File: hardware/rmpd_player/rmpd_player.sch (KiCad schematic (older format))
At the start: 54 parts

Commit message: ds3231 stubs added
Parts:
- added BT?: CR2032, symbol Device:Battery_Cell
- added C?: 100n, symbol Device:C
- added U?: DS3231M, Package_SO:SOIC-16W_7.5x10.3mm_P1.27mm, symbol Timer_RTC:DS3231M
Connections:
- net labels added: I2C_SCL, I2C_SDA, TRANSIENT_MUTE
- net labels removed: MUTE
- wire segments 235 -> 247
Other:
- moved on the sheet: R?

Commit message: annotate schematic
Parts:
- removed J?: Micro_SD_Card_Det, symbol Connector:Micro_SD_Card_Det
- removed J?: AudioJack3_Ground, symbol Connector:AudioJack3_Ground
- added J2: PROG, Pin_Headers:Pin_Header_Straight_1x06_Pitch2.54mm, symbol Connector_Generic:Conn_01x06
- added J3: LINE_OUT_INT, Pin_Headers:Pin_Header_Straight_1x04_Pitch2.54mm, symbol Connector_Generic:Conn_01x04
- added J4: LINE_OUT_R, symbol Connector:Conn_Coaxial
- added J5: MICRO_SD, microsd:Conn_uSDcard, symbol Connector:Micro_SD_Card
- added J6: LINE_OUT_L, symbol Connector:Conn_Coaxial
- BT1: renamed from BT?; footprint (none) -> Battery_Holders:Keystone_103_1x20mm-CoinCell
- C1, C10, C11, C13, C14, C16, C2, C3, C4, C5, C6, C7, C8, C9: renamed from C?; footprint (none) -> Capacitors_SMD:C_0805_HandSoldering
- C12, C15, C17, C18: renamed from C?; footprint (none) -> Capacitors_THT:CP_Radial_D5.0mm_P2.50mm
- D1: renamed from D?; footprint (none) -> Diodes_SMD:D_0805
- F1: renamed from F?; footprint (none) -> Fuse_Holders_and_Fuses:Fuse_SMD1206_HandSoldering
- J1: renamed from J?; value Barrel_Jack -> POWER; footprint (none) -> Connectors:BARREL_JACK
- R1, R10, R11, R12, R13, R14, R15, R16, R17, R18, R19, R2, R20, R21, R22, R23, R24, R3, R4, R5, R6, R7, R8, R9: renamed from R?; footprint (none) -> Resistors_SMD:R_0805_HandSoldering
- U3: renamed from U?; footprint (none) -> TO_SOT_Packages_SMD:SOT-223
- Y1: renamed from Y?; footprint (none) -> Crystals:Crystal_HC18-U_Vertical
- gave numbers to parts that had none: 7
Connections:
- net labels added: EN, IO0, UART_RX, UART_TX
- wire segments 247 -> 268
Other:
- moved on the sheet: BT1, C3, U1

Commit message: 2rca footprints
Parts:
- removed J4: LINE_OUT_R, symbol Connector:Conn_Coaxial
- removed J6: LINE_OUT_L, symbol Connector:Conn_Coaxial
- added J4: LINE_OUT, microsd:2RCA, symbol Connector:Conn_Coaxial_x2
- Q1, Q2, Q3, Q4: footprint Package_TO_SOT_SMD:SOT-23 -> TO_SOT_Packages_SMD:SOT-23
- U1: footprint Package_SO:SOIC-16W_7.5x10.3mm_P1.27mm -> Housings_SOIC:SOIC-16W_7.5x10.3mm_Pitch1.27mm
- U4: footprint ESP32-footprints-Lib:ESP32-WROOM -> microsd:ESP32-WROOM
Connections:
- wire segments 268 -> 264
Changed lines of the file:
@@
 F 0 "U4" H 5975 3587 60  0000 C CNN
 F 1 "ESP32-WROOM" H 5975 3481 60  0000 C CNN
-F 2 "ESP32-footprints-Lib:ESP32-WROOM" H 6350 3550 60  0001 C CNN
+F 2 "microsd:ESP32-WROOM" H 6350 3550 60  0001 C CNN
 F 3 "" H 5550 2650 60  0001 C CNN
 	1    6000 2200
@@
 	6600 5950 6450 5950
 Connection ~ 6450 5950
-Wire Wire Line
-	6600 4400 6700 4400
-Wire Wire Line
-	6700 4400 6700 4550
-Wire Wire Line
-	6700 4550 6750 4550
 Connection ~ 6600 4400
-Wire Wire Line
-	6450 5100 6700 5100
 Connection ~ 6450 5100
-Wire Wire Line
-	6600 5950 6950 5950
-Wire Wire Line
-	6950 5950 6950 5450
 Connection ~ 6600 5950
 $Comp
@@
 F 0 "Q1" H 8190 4746 50  0000 L CNN
 F 1 "BC848" H 8190 4655 50  0000 L CNN
-F 2 "Package_TO_SOT_SMD:SOT-23" H 8200 4625 50  0001 L CIN
+F 2 "TO_SOT_Packages_SMD:SOT-23" H 8200 4625 50  0001 L CIN
 F 3 "http://www.infineon.com/dgdl/Infineon-BC847SERIES_BC848SERIES_BC849SERIES_BC850SERIES-DS-v01_01-en.pdf?fileId=db3a304314dca389011541d4630a1657" H 8000 4700 50  0001 L CNN
 	1    8000 4700
@@
 F 0 "Q2" H 8590 5646 50  0000 L CNN
 F 1 "BC848" H 8590 5555 50  0000 L CNN
-F 2 "Package_TO_SOT_SMD:SOT-23" H 8600 5525 50  0001 L CIN
+F 2 "TO_SOT_Packages_SMD:SOT-23" H 8600 5525 50  0001 L CIN
 F 3 "http://www.infineon.com/dgdl/Infineon-BC847SERIES_BC848SERIES_BC849SERIES_BC850SERIES-DS-v01_01-en.pdf?fileId=db3a304314dca389011541d4630a1657" H 8400 5600 50  0001 L CNN
 	1    8400 5600
@@
 $EndComp
 Wire Wire Line
-	6700 4400 7900 4400
-Wire Wire Line
 	7900 4400 7900 4500
-Connection ~ 6700 4400
 Wire Wire Line
 	8300 5400 8300 5100
-Wire Wire Line
-	7900 5950 7250 5950
-Connection ~ 6950 5950
 Wire Wire Line
 	8300 5800 8300 5950
@@
 F 0 "Q3" H 8890 4354 50  0000 L CNN
 F 1 "BC858" H 8890 4445 50  0000 L CNN
-F 2 "Package_TO_SOT_SMD:SOT-23" H 8900 4325 50  0001 L CIN
+F 2 "TO_SOT_Packages_SMD:SOT-23" H 8900 4325 50  0001 L CIN
 F 3 "http://www.fairchildsemi.com/ds/BC/BC856.pdf" H 8700 4400 50  0001 L CNN
 	1    8700 4400
@@
 F 0 "Q4" H 9290 5254 50  0000 L CNN
 F 1 "BC858" H 9290 5345 50  0000 L CNN
-F 2 "Package_TO_SOT_SMD:SOT-23" H 9300 5225 50  0001 L CIN
+F 2 "TO_SOT_Packages_SMD:SOT-23" H 9300 5225 50  0001 L CIN
 F 3 "http://www.fairchildsemi.com/ds/BC/BC856.pdf" H 9100 5300 50  0001 L CNN
 	1    9100 5300
@@
 F 0 "U1" H 1650 1250 50  0000 C CNN
 F 1 "DS3231M" H 1650 1150 50  0000 C CNN
-F 2 "Package_SO:SOIC-16W_7.5x10.3mm_P1.27mm" H 1950 1000 50  0001 C CNN
+F 2 "Housings_SOIC:SOIC-16W_7.5x10.3mm_Pitch1.27mm" H 1950 1000 50  0001 C CNN
 F 3 "http://datasheets.maximintegrated.com/en/ds/DS3231.pdf" H 2220 1650 50  0001 C CNN
 	1    1950 1600
@@
 	1    0    0    -1
 $EndComp
-$Comp
-L Connector:Conn_Coaxial J4
-U 1 1 5C0DDCCD
-P 6950 4550
-F 0 "J4" H 6950 4850 50  0000 L CNN
-F 1 "LINE_OUT_R" H 6800 4750 50  0000 L CNN
-F 2 "" H 6950 4550 50  0001 C CNN
-F 3 " ~" H 6950 4550 50  0001 C CNN
-	1    6950 4550
-	1    0    0    -1
-$EndComp
-$Comp
-L Connector:Conn_Coaxial J6
-U 1 1 5C0DDDB1
-P 6950 5250
-F 0 "J6" H 6900 5550 50  0000 L CNN
-F 1 "LINE_OUT_L" H 6800 5450 50  0000 L CNN
-F 2 "" H 6950 5250 50  0001 C CNN
-F 3 " ~" H 6950 5250 50  0001 C CNN
-	1    6950 5250
-	1    0    0    -1
-$EndComp
-Wire Wire Line
-	6750 5250 6700 5250
-Wire Wire Line
-	6700 5250 6700 5100
-Connection ~ 6700 5100
-Wire Wire Line
-	6700 5100 8300 5100
-Wire Wire Line
-	6950 4750 6950 4800
-Wire Wire Line
-	6950 4800 7250 4800
-Wire Wire Line
-	7250 4800 7250 5950
-Connection ~ 7250 5950
-Wire Wire Line
-	7250 5950 6950 5950
+Wire Wire Line
+	6600 4400 6750 4400
+Wire Wire Line
+	6600 5950 7100 5950
+Wire Wire Line
+	6450 5100 6750 5100
+$Comp
+L Connector:Conn_Coaxial_x2 J4
+U 1 1 5C0CC33D
+P 7100 4650
+F 0 "J4" H 7200 4450 50  0000 L CNN
+F 1 "LINE_OUT" H 7200 4350 50  0000 L CNN
+F 2 "microsd:2RCA" H 7100 4550 50  0001 C CNN
+F 3 " ~" H 7100 4550 50  0001 C CNN
+	1    7100 4650
+	1    0    0    -1
+$EndComp
+Wire Wire Line
+	6900 4550 6750 4550
+Wire Wire Line
+	6750 4550 6750 4400
+Connection ~ 6750 4400
+Wire Wire Line
+	6750 4400 7900 4400
+Wire Wire Line
+	6900 4750 6750 4750
+Wire Wire Line
+	6750 4750 6750 5100
+Connection ~ 6750 5100
+Wire Wire Line
+	6750 5100 8300 5100
+Wire Wire Line
+	7100 4950 7100 5950
+Connection ~ 7100 5950
+Wire Wire Line
+	7100 5950 7900 5950
 $EndSCHEMATC

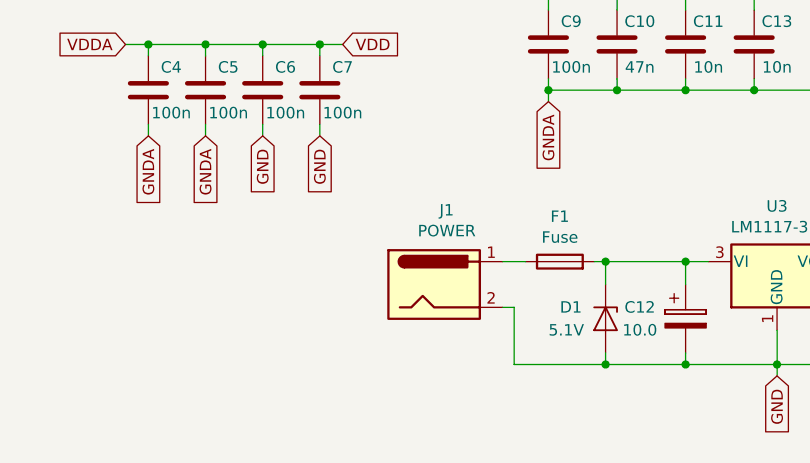
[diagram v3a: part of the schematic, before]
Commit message: power_int pinheader
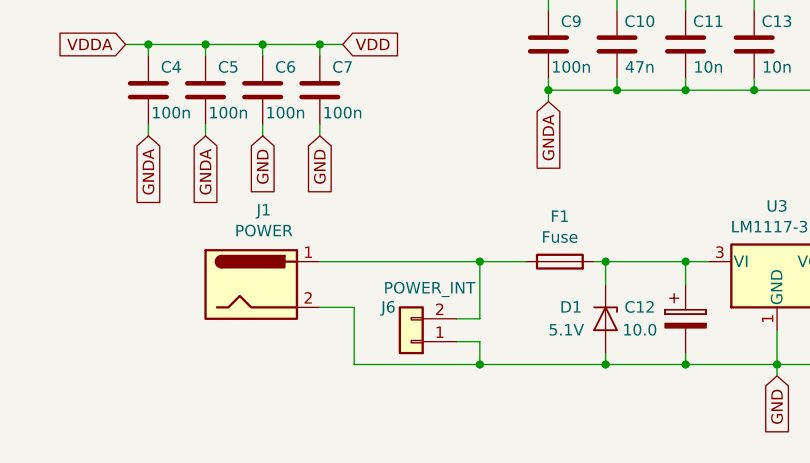
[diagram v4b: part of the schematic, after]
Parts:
- added J6: POWER_INT, Pin_Headers:Pin_Header_Straight_1x02_Pitch2.54mm, symbol Connector_Generic:Conn_01x02
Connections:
- net GND: now also J6.1 (Pin_1)
- net at F1.1, J1.1: now also J6.2 (Pin_2)
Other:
- moved on the sheet: J1
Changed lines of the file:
@@
 L Connector:Barrel_Jack J1
 U 1 1 5C11E4C3
-P 3950 6800
-F 0 "J1" H 4005 7125 50  0000 C CNN
-F 1 "POWER" H 4005 7034 50  0000 C CNN
-F 2 "Connectors:BARREL_JACK" H 4000 6760 50  0001 C CNN
-F 3 "~" H 4000 6760 50  0001 C CNN
-	1    3950 6800
+P 3150 6800
+F 0 "J1" H 3205 7125 50  0000 C CNN
+F 1 "POWER" H 3205 7034 50  0000 C CNN
+F 2 "Connectors:BARREL_JACK" H 3200 6760 50  0001 C CNN
+F 3 "~" H 3200 6760 50  0001 C CNN
+	1    3150 6800
 	1    0    0    -1
 $EndComp
 Connection ~ 5050 6700
 Wire Wire Line
-	4250 6900 4300 6900
-Wire Wire Line
-	4300 6900 4300 7150
+	3450 6900 3600 6900
+Wire Wire Line
+	3600 6900 3600 7150
 Connection ~ 5050 7150
 Wire Wire Line
-	4250 6700 4350 6700
-Wire Wire Line
-	4300 7150 4700 7150
+	3450 6700 4150 6700
+Wire Wire Line
+	3600 7150 4150 7150
 $Comp
 L Device:Fuse F1
@@
 Wire Wire Line
 	7100 5950 7900 5950
+$Comp
+L Connector_Generic:Conn_01x02 J6
+U 1 1 5C0E4996
+P 3850 7050
+F 0 "J6" H 3950 6900 50  0000 C CNN
+F 1 "POWER_INT" H 3770 6816 50  0000 C CNN
+F 2 "Pin_Headers:Pin_Header_Straight_1x02_Pitch2.54mm" H 3850 7050 50  0001 C CNN
+F 3 "~" H 3850 7050 50  0001 C CNN
+	1    3850 7050
+	-1   0    0    1
+$EndComp
+Wire Wire Line
+	4050 7050 4150 7050
+Wire Wire Line
+	4150 7050 4150 7150
+Connection ~ 4150 7150
+Wire Wire Line
+	4150 7150 4700 7150
+Wire Wire Line
+	4050 6950 4150 6950
+Wire Wire Line
+	4150 6950 4150 6700
+Connection ~ 4150 6700
+Wire Wire Line
+	4150 6700 4350 6700
 $EndSCHEMATC

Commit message: tht diode
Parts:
- D1: footprint Diodes_SMD:D_0805 -> Diodes_THT:D_A-405_P7.62mm_Horizontal
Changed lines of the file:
@@
 F 0 "D1" V 4650 6750 50  0000 L CNN
 F 1 "5.1V" V 4750 6700 50  0000 L CNN
-F 2 "Diodes_SMD:D_0805" H 4700 6950 50  0001 C CNN
+F 2 "Diodes_THT:D_A-405_P7.62mm_Horizontal" H 4700 6950 50  0001 C CNN
 F 3 "~" H 4700 6950 50  0001 C CNN
 	1    4700 6950

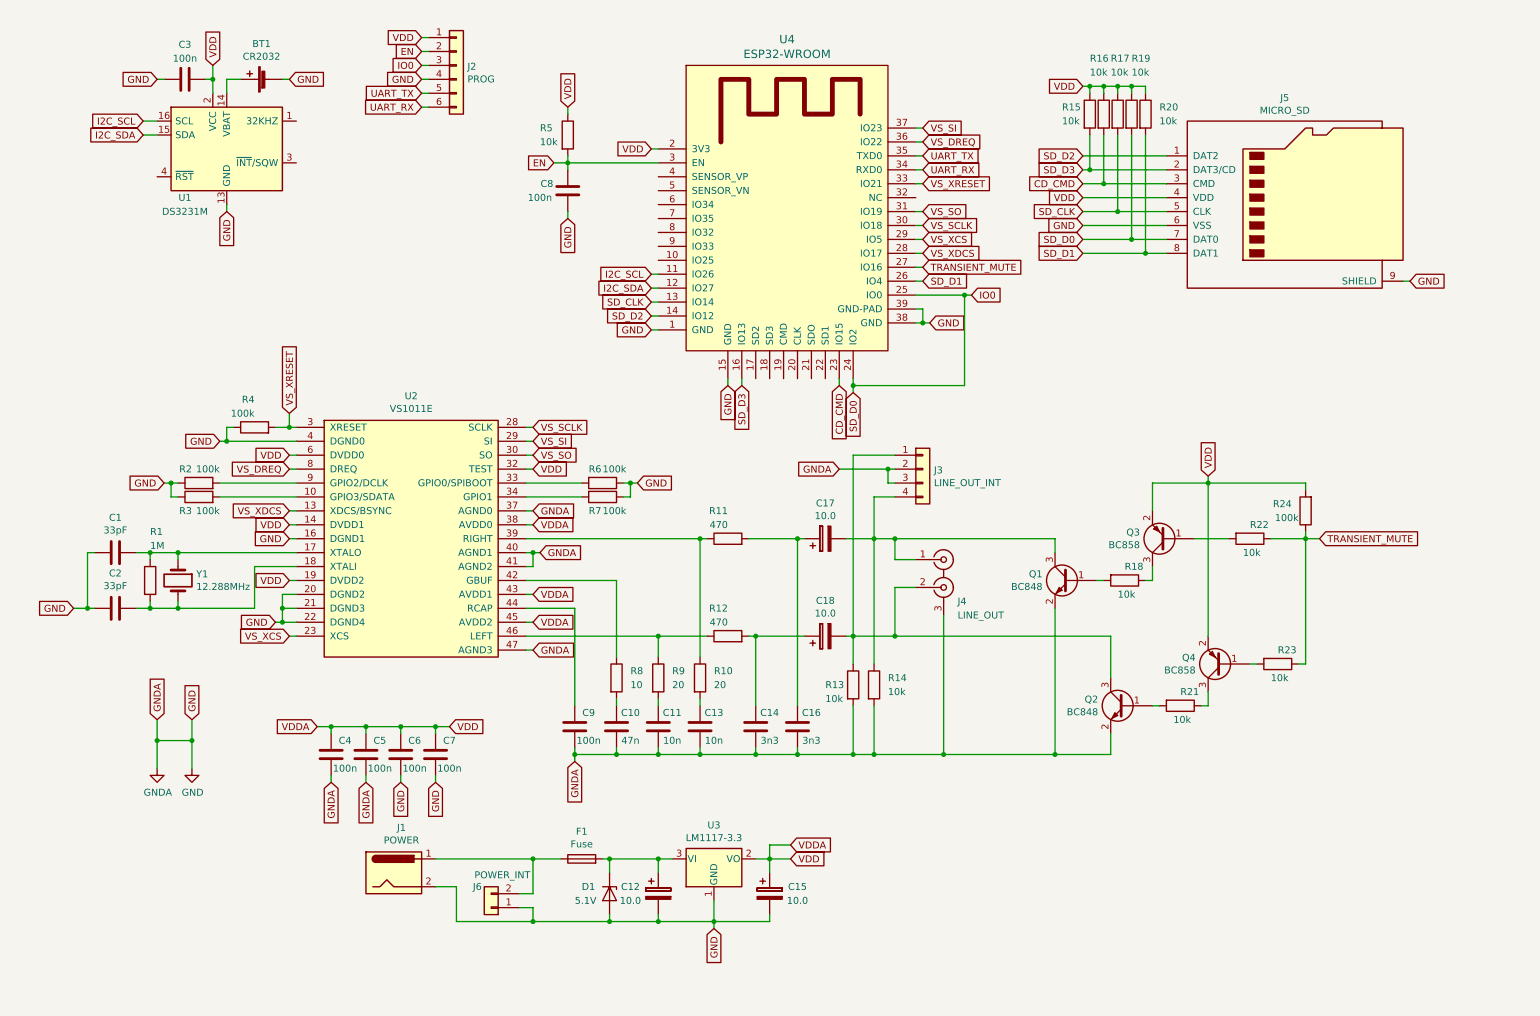
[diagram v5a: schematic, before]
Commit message: schematic op amp buffer added
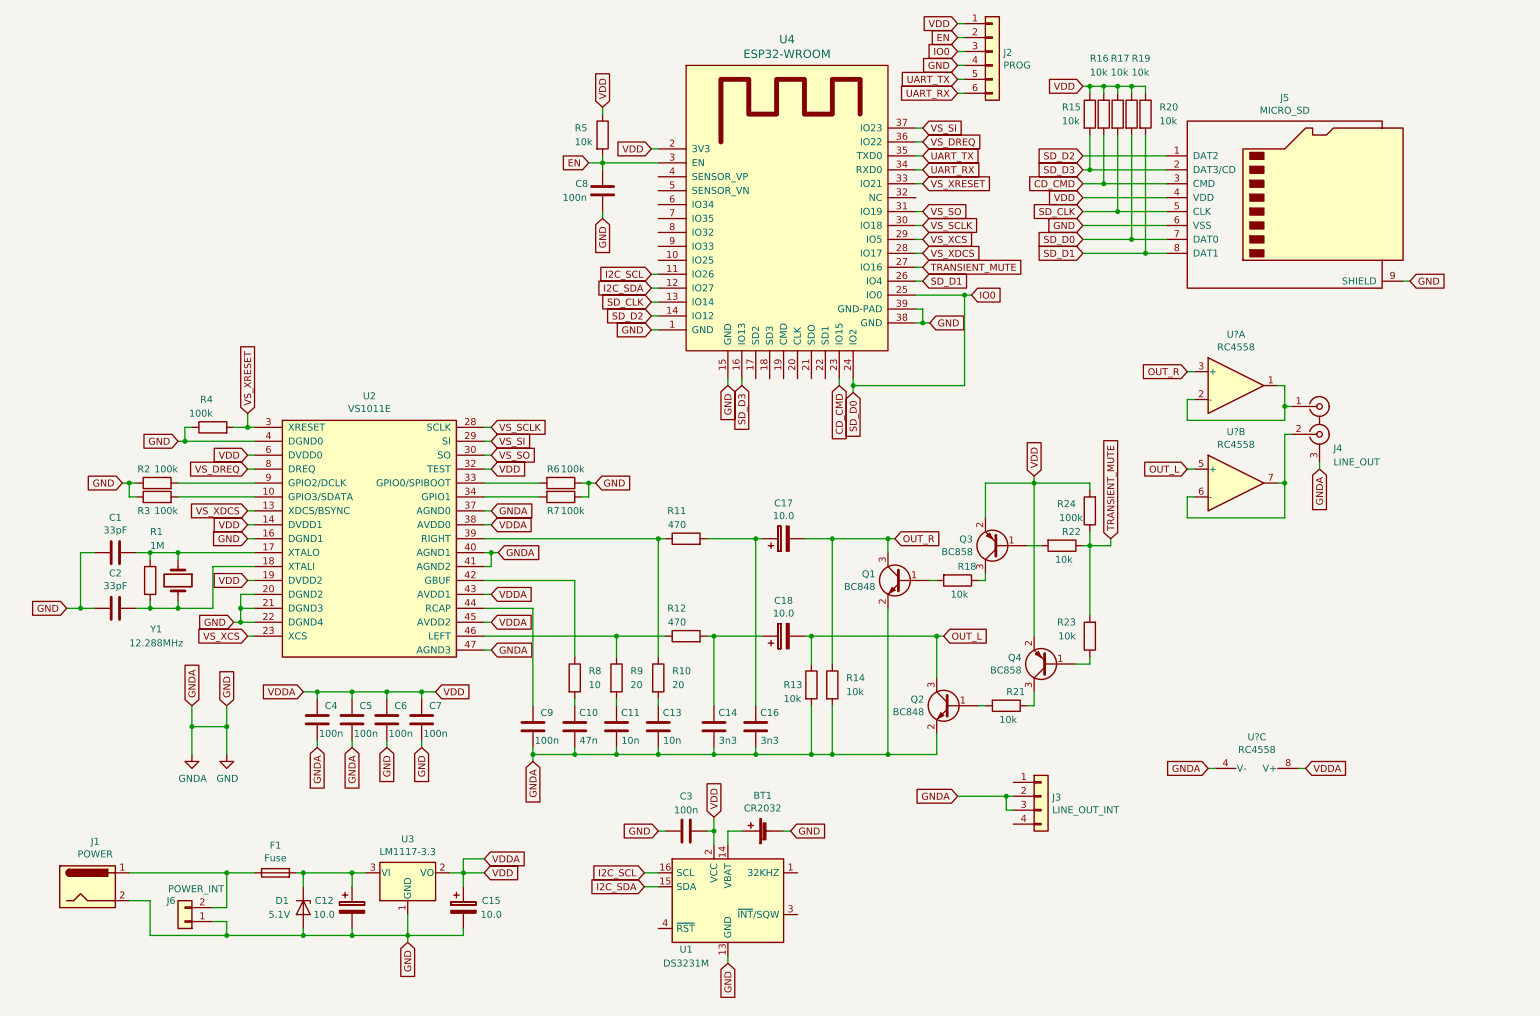
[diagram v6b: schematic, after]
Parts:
- added U? (x3): RC4558, symbol Amplifier_Operational:RC4558
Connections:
- net GND: now also U?.4 (V-)
- net TRANSIENT_MUTE: now also R23.2; no longer R23.1
- net VDD: now also U?.8 (V+)
- net OUT_R: now reaches C17.2, Q1.3 (C), R14.1
- net OUT_R: now also U?.3 (+); no longer J3.4 (Pin_4), J4.1 (IN1)
- net OUT_L: now reaches C18.2, Q2.3 (C), R13.1
- net OUT_L: now also U?.5 (+); no longer J3.1 (Pin_1), J4.2 (IN2)
- net at Q4.1 (B): now also R23.1; no longer R23.2
- new net: J4.1 (IN1), U?.1, U?.2 (-)
- new net: J4.2 (IN2), U?.6 (-), U?.7
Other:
- moved on the sheet: BT1, C10, C11, C12, C13, C14, C15, C16, C17, C18, C3, C4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
